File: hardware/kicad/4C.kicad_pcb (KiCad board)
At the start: 4 copper layers, 100 x 100 mm, 202 parts, among them J1 Conn_01x04, J10 Conn_01x02, J11 Conn_01x02, J12 Conn_01x02, J13 Conn_01x02, J18 Conn_01x04, J19 Conn_01x04, J2 XT90PW-F, J20 Conn_01x04, J21 Conn_01x04, J22 Conn_01x03, J25 USB_C_Receptacle_USB2.0_16P, Q1 CSD18532Q5B, Q10 CSD18532Q5B, Q11 CSD18532Q5B, Q12 CSD18532Q5B, Q13 CSD18532Q5B, Q14 CSD18532Q5B, Q15 CSD18532Q5B, Q16 CSD18532Q5B, Q2 CSD18532Q5B, Q3 CSD18532Q5B, Q4 CSD18532Q5B, Q5 CSD18532Q5B, Q6 CSD18532Q5B, Q7 CSD18532Q5B, Q8 CSD18532Q5B, Q9 CSD18532Q5B, U1 DRV8701ERGER, U2 DRV8701ERGER, U3 DRV8701ERGER, U4 DRV8701ERGER, U5 STM32G474RETx, U6 AMS1117-3.3

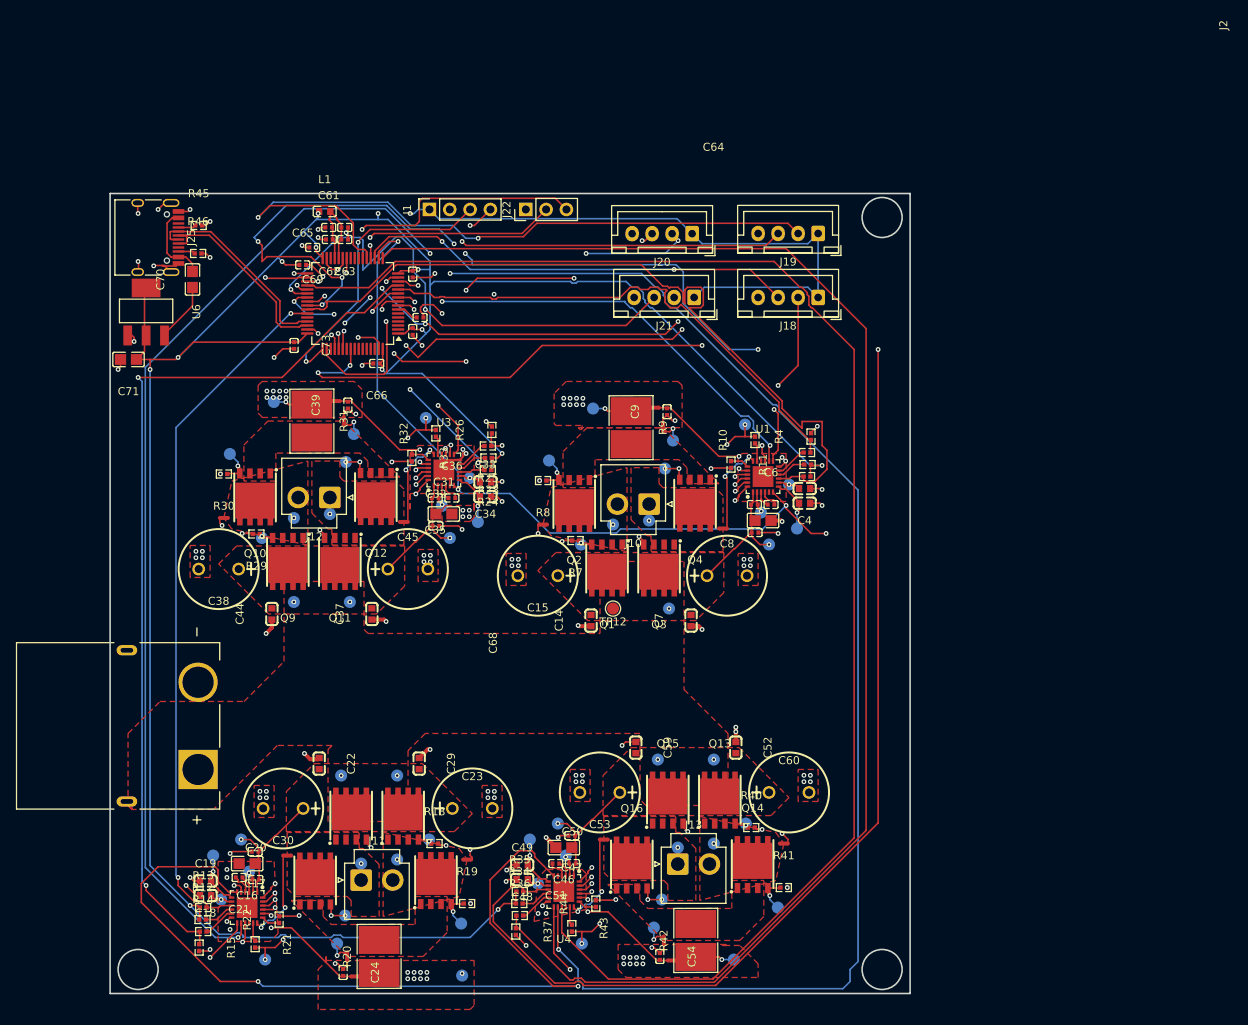
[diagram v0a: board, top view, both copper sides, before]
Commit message: fixed xt90 footprint for pigtails
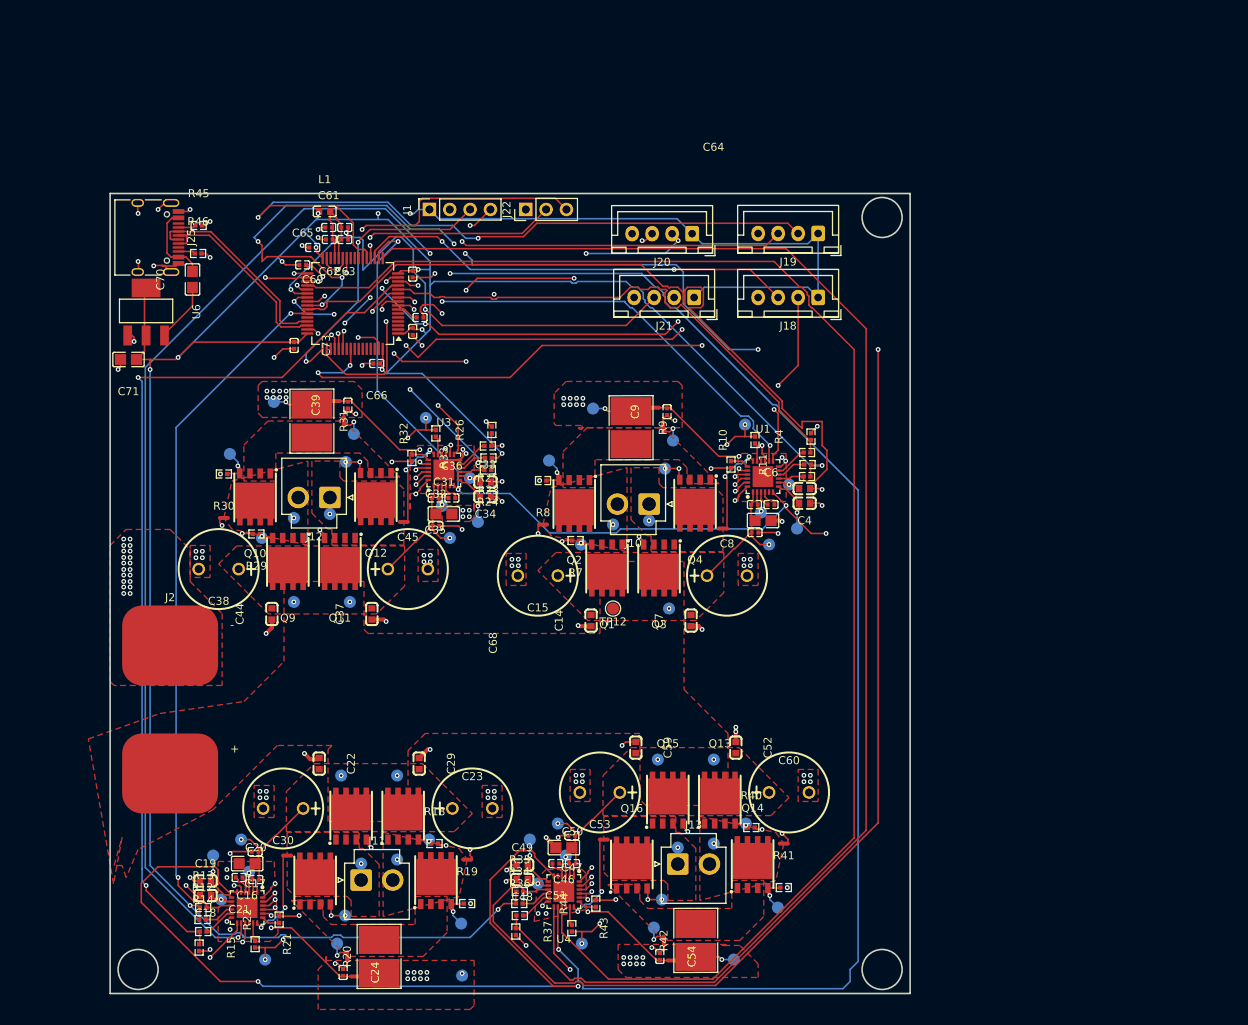
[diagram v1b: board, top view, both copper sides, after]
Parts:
- J2: value XT90PW-F -> Conn_01x02; footprint Easyeda:AMASS_XT90PW-F -> Connector_Wire:SolderWirePad_2x01_SMD_10x12mm
- moved J2 11.4 mm to (112.5, 108.0), turned to 0 degrees
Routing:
- net GND: vias 134 -> 154

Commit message: Completed v0 board
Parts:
- added TP57: TestPoint, TestPoint:TestPoint_Pad_D1.5mm, B.Cu at (118.0, 62.2)
- added TP58: TestPoint, TestPoint:TestPoint_Pad_D1.5mm, B.Cu at (123.2, 67.8)
- C20, C35, C5, C50: value C1608X7R1C105K -> CL05A105KA5NQNC
- C61, C63: value GRM188R70J105KA01D -> CL05A105KA5NQNC
- J22: value Conn_01x03 -> Conn_01x04; footprint Connector_PinHeader_2.54mm:PinHeader_1x03_P2.54mm_Vertical -> Connector_JST:JST_GH_SM04B-GHS-TB_1x04-1MP_P1.25mm_Horizontal
- Q1, Q10, Q11, Q12, Q13, Q14, Q15, Q16, Q2, Q3, Q4, Q5, Q6, Q7, Q8, Q9: value CSD18532Q5B -> CSD18540Q5B
- TP12: moved to B.Cu
- moved J22 3.52 mm to (160.2, 54.8), turned to 180 degrees
- moved J2 2.21 mm to (111.6, 110.0)
- moved TP12 0.72 mm to (167.5, 104.0), turned to 0 degrees
- moved J12 0.30 mm to (132.3, 89.3)
- moved C63 0.09 mm to (134.4, 57.2)
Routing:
- net VM: track 64.0 -> 40.8 mm, vias 11 -> 32
- net +3.3V: track 395.8 -> 401.4 mm, vias 14 -> 16
- net +5V: track 10.2 -> 14.1 mm, vias 0 -> 1
- net /UART_TX: track 48.3 -> 51.9 mm, vias 2 -> 4
- net /ENC_2_B: track 90.5 -> 93.9 mm
- net /UART_RX: track 42.7 -> 45.8 mm, vias 2 -> 4
- net /SO_4: track 184.0 -> 186.5 mm
- net GND: track 124.6 -> 126.1 mm, vias 154 -> 155
- net /ENC_2_A: track 54.1 -> 55.4 mm
- net /nSLEEP: track 363.3 -> 363.8 mm
- added copper zone on B.Cu, net VM
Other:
- board text added: "AVDD"
- board text added: "DVDD"
- board text added: "ENC 1"
- board text added: "ENC 2"
- board text added: "ENC 3"
- board text added: "ENC 4"
- board text added: "GH1"
- board text added: "GH2"
- board text added: "GL1"
- board text added: "GL2"
- board text added: "GND"
- board text added: "M1"
- board text added: "M2"
- board text added: "M3"
- board text added: "M4"
- board text added: "OUT_1"
- board text added: "OUT_2"
- board text added: "SHUNT_TOP"
- board text added: "VCP"
- board text added: "VM"
